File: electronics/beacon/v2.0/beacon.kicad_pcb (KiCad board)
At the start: 2 copper layers, 10 x 22 mm, 15 parts, among them J1 L, J2 R, J3 TPI, Q1 BSS138, U1 ATTINY10-TS, U2 MIC5225-1.8YM5

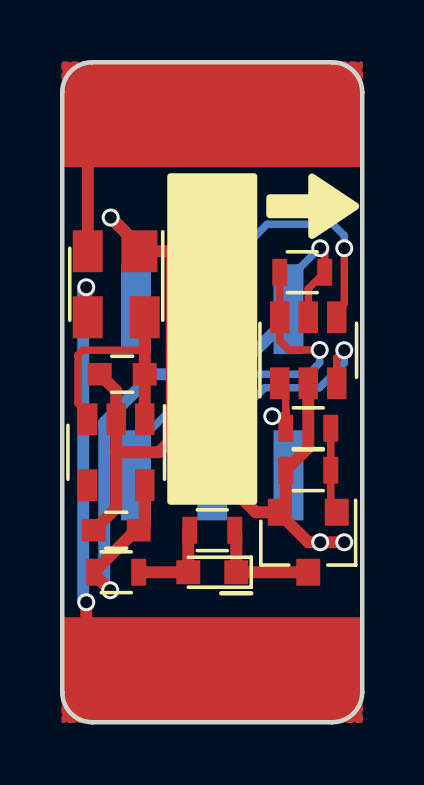
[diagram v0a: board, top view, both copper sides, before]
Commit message: electronics: beacon: Add solder jumper to v2.0
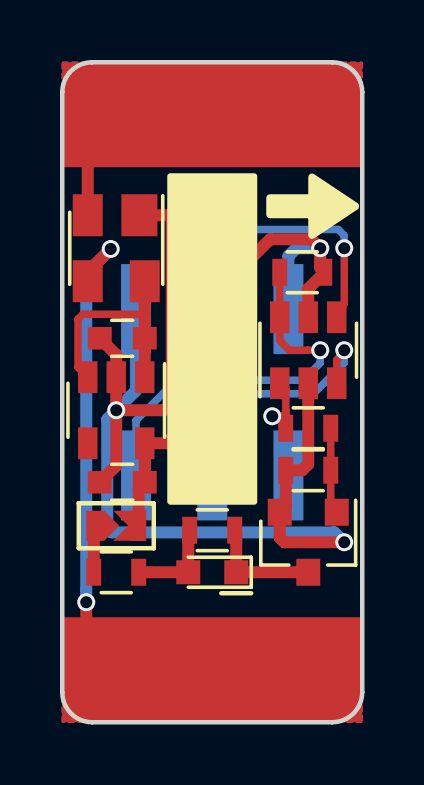
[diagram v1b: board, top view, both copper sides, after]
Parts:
- added JP1: +1V8, bcan:Solder_Jumper_NC_Small, F.Cu at (146.8, 104.5)
- moved C2 1.61 mm to (147.0, 103.0)
- moved U2 1.40 mm to (146.8, 100.6)
- moved C1 1.20 mm to (147.0, 98.2)
- moved D2 1.20 mm to (146.8, 95.2)
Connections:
- R4 pad 1: +1V8 -> Net-(JP1-Pad1)
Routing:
- net GND: track 31.9 -> 38.4 mm, vias 3 -> 2
- net +1V8: track 23.1 -> 19.9 mm, vias 2 -> 1
- net Net-(JP1-Pad1): track 0.00 -> 2.41 mm
- net /RAIL_L: track 8.70 -> 6.56 mm
- net /RAIL_R: track 18.0 -> 19.2 mm
- net /~RST: track 12.4 -> 13.0 mm
